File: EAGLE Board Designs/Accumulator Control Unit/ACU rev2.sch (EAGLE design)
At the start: 134 parts, among them J1 CONNECTOR-CAN_NF_T_V_BLACK, J2 CONNECTOR-6_MF_T_V_, J3 CONNECTOR-8_MF_T_V_, Q1 TRANSISTOR_N_MOS__PMV15ENEA, T1 TRANSFORMER_HM2112ZNLT_AIRGAP, U1 VOLTAGE_REGULATOR_SOT89_12V, U10 OPAMP_1_CHANNEL_OPA991, U11 LOGICGATE_AND_DCK3, U12 OPAMP_1_CHANNEL_OPA991, U13 OPAMP_1_CHANNEL_OPA991, U14 OPAMP_1_CHANNEL_OPA991, U15 LOGICGATE_AND_DCK3, U16 OPAMP_1_CHANNEL_OPA991, U17 OPAMP_1_CHANNEL_OPA991, U18 OPAMP_1_CHANNEL_OPA991, U19 ADC128S022, U2 ADG1423, U24 ADM823, U25 TCAN1051HQV-Q1, U3 LM555, U4 OPAMP_1_CHANNEL_OPA991, U5 MAX7400, U6 MAX7400, U7 OPAMP_1_CHANNEL_OPA991, U8 LOGICGATE_AND_DCK3, U9 OPAMP_1_CHANNEL_OPA991

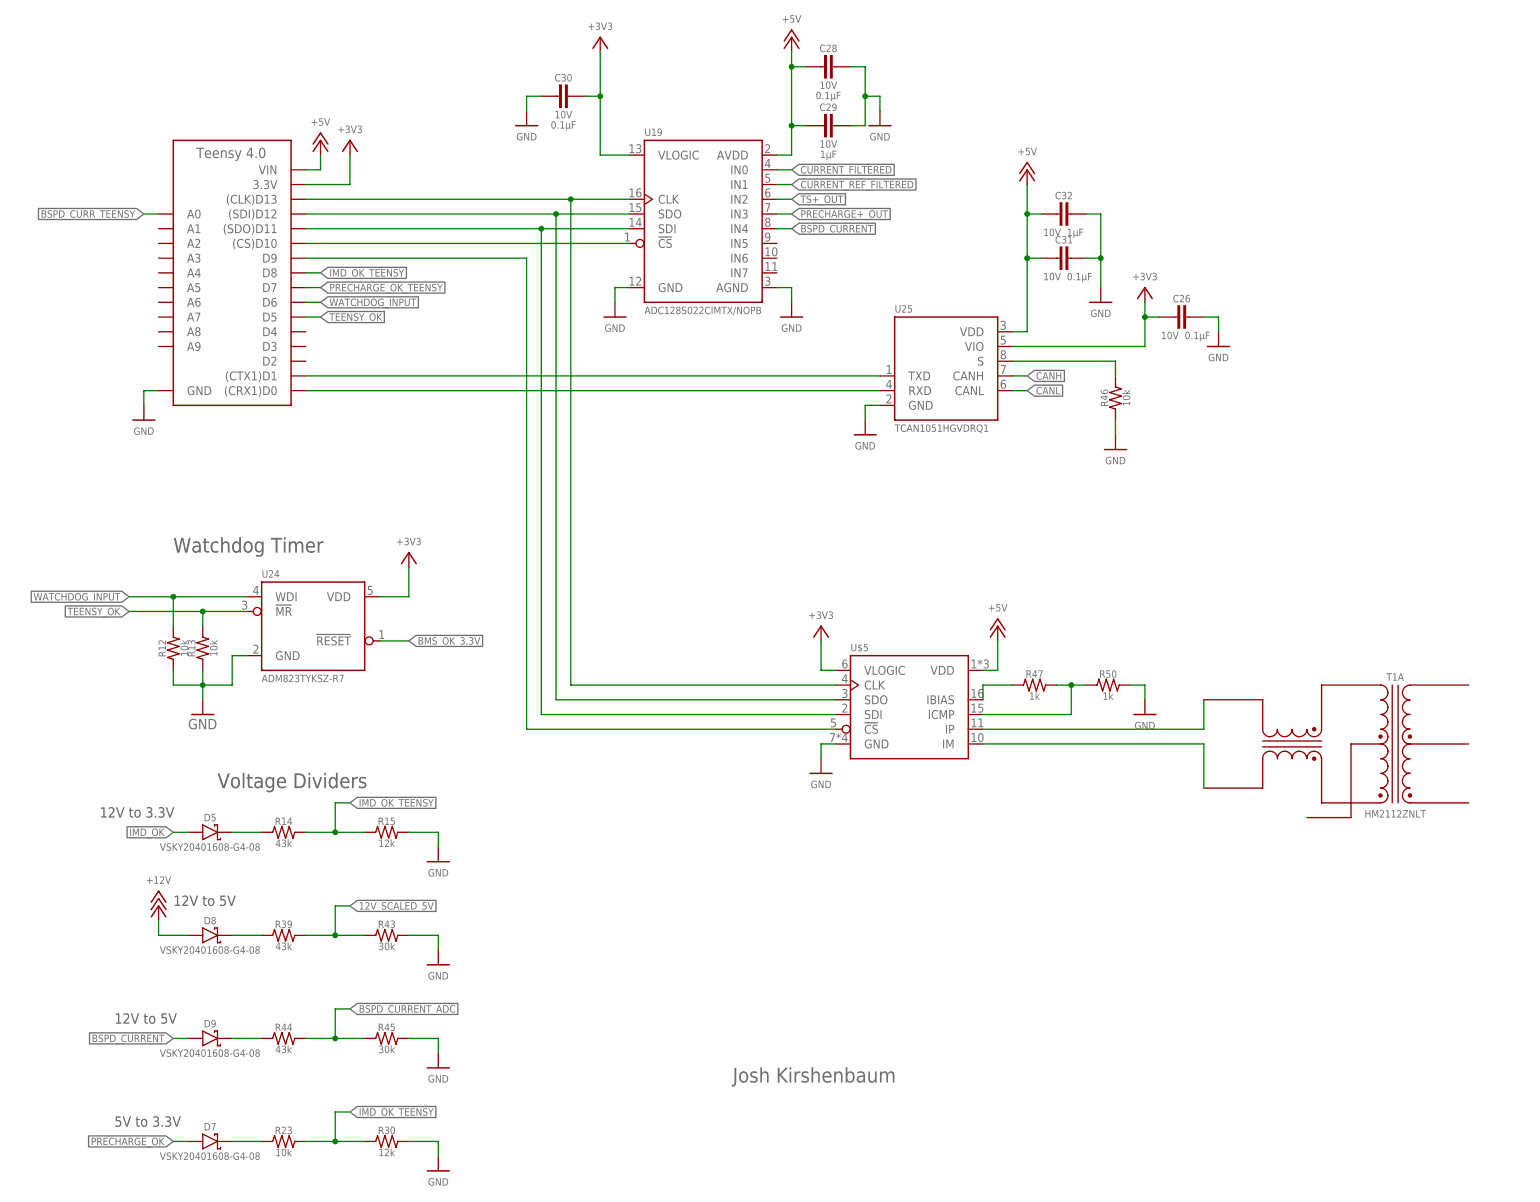
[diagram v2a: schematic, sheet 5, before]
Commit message: add ltc6820 and transformer
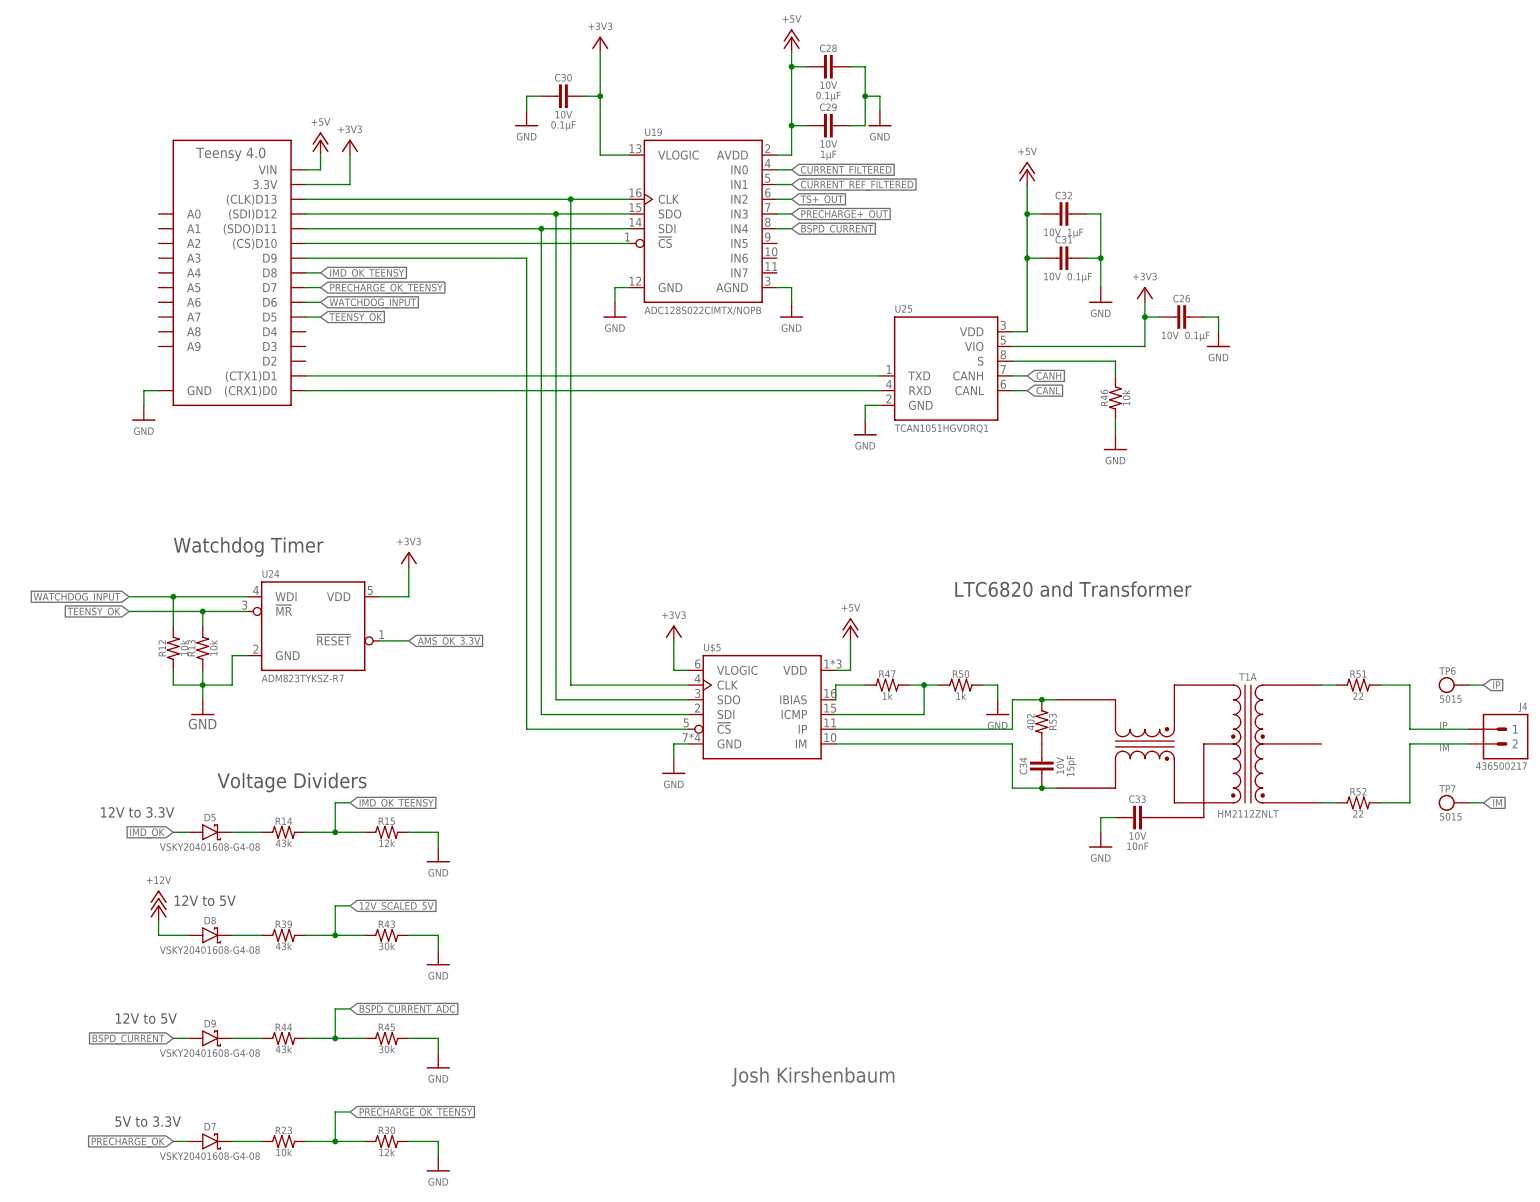
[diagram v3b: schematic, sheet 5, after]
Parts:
- added C33: CAPACITOR_0603_10V_10NF, HyTechDevices - Copy:CAPACITOR_0603_10V_10NF
- added C34: CAPACITOR_0603_10V_15PF, HyTechDevices - Copy:CAPACITOR_0603_10V_15PF
- added J4: CONNECTOR-2_MF_T_V_, HyTechDevices - Copy:CONNECTOR-2_MF_T_V_
- added R51, R52: RESISTOR_0603_22, HyTechDevices - Copy:RESISTOR_0603_22
- added R53: RESISTOR_0603_402, HyTechDevices - Copy:RESISTOR_0603_402
- added TP6, TP7: TEST_POINT, HyTechDevices - Copy:TEST_POINT
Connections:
- net BMS_OK_3.3V renamed AMS_OK_3.3V
- removed net BMS_OK: U$13.P$1, U$9.CONTACT1
- removed net BSPD_CURR_TEENSY: A1.A0
- removed net N$19: U$2.12
- removed net N$20: U$2.11
- removed net N$21: U$2.10
- removed net N$4: TP3.P$1
- new net IM: J4.2, R52.2, TP7.P$1
- new net IP: J4.1, R51.2, TP6.P$1
- new net N$39: C33.1, T1A.TCT
- new net N$40: R51.1, T1A.MX-
- new net N$41: R52.1, T1A.MX+
- new net N$42: C34.1, R53.2
- net +3V3: now also TP3.P$1
- net AMS_OK: now also U$13.P$1, U$9.CONTACT1
- net GND: now also C33.2, U$2.10, U$2.11, U$2.12
- net IMD_OK_TEENSY: no longer R23.2, R30.1
- net N$35: now also R53.1
- net N$38: now also C34.2
- net PRECHARGE_OK_TEENSY: now also R23.2, R30.1
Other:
- note added: "LTC6820 and Transformer"
- moved on the sheet: R47, R50, T1A, U$5
